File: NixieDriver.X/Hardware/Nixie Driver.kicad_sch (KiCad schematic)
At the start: 5 parts, among them J1 Conn_02x03_Odd_Even, J2 Conn_02x03_Odd_Even, J3 Conn_01x03, U1 PIC16F15243

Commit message: STM32L011F4U MCU
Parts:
- removed J1: Conn_02x03_Odd_Even, Connector_PinHeader_2.54mm:PinHeader_1x03_P2.54mm_Vertical, symbol Connector_Generic:Conn_01x03
- removed J2: Conn_02x03_Odd_Even, Connector_PinHeader_2.54mm:PinHeader_1x04_P2.54mm_Vertical, symbol Connector_Generic:Conn_01x04
- removed U1: PIC16F15243, Package_DFN_QFN:VQFN-20-1EP_3x3mm_P0.4mm_EP1.7x1.7mm, symbol MCU_Microchip_PIC16_:PIC16F15243-E/REB
- added J1: SWD, Connectory_PCB_Edge_:Tag-Connect EVC3-06, symbol Connector_Generic:Conn_01x06
- added J4, J5: Conn_01x03, Connector_PinHeader_2.54mm:PinHeader_1x02_P2.54mm_Vertical, symbol Connector_Generic:Conn_01x02
- added R13: 2.2k, Resistor_SMD:R_0603_1608Metric, symbol Device:R_US
- added U2: STM32L011F4Ux, Package_DFN_QFN:ST_UFQFPN-20_3x3mm_P0.5mm, symbol MCU_ST_STM32L0:STM32L011F4Ux
- J3: footprint Connector_PinHeader_2.54mm:PinHeader_1x03_P2.54mm_Vertical -> Connector_PinHeader_2.54mm:PinHeader_1x02_P2.54mm_Vertical; symbol Connector_Generic:Conn_01x03 -> Connector_Generic:Conn_01x02
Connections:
- net Driver_0: now also U2.9 (PA6)
- net Driver_1: now also U2.7 (PA4)
- net Driver_2: now also U2.6 (PA1)
- net Driver_3: now also U2.5 (PA0)
- net Driver_4: now also U2.1 (PC14)
- net Driver_5: now also U2.20 (PB9)
- net Driver_6: now also U2.15 (PA10)
- net Driver_7: now also U2.14 (PA9)
- net Driver_8: now also U2.11 (PB1)
- net Driver_9: now also U2.10 (PA7)
- net Driver_Dot: now also U2.8 (PA5)
- net GND: now also J1.5 (Pin_5), U2.12 (VSS)
- net SCL: now also J4.2 (Pin_2), U2.18 (PB6)
- net SDA: now also J4.1 (Pin_1), U2.19 (PB7)
- net Vdd: now also J1.1 (Pin_1), J5.1 (Pin_1), R13.2, U2.13 (VDD), U2.4 (VDDA); no longer J3.2 (Pin_2)
- net Vnn: now also J3.2 (Pin_2); no longer J3.3 (Pin_3)
- new net ADDR: J5.2 (Pin_2), R13.1, U2.2 (PC15)
- new net NRST: J1.3 (Pin_3), U2.3 (NRST)
- new net SWCLK: J1.4 (Pin_4), U2.17 (PA14)
- new net SWDIO: J1.2 (Pin_2), U2.16 (PA13)
- new net SWO: J1.6 (Pin_6)

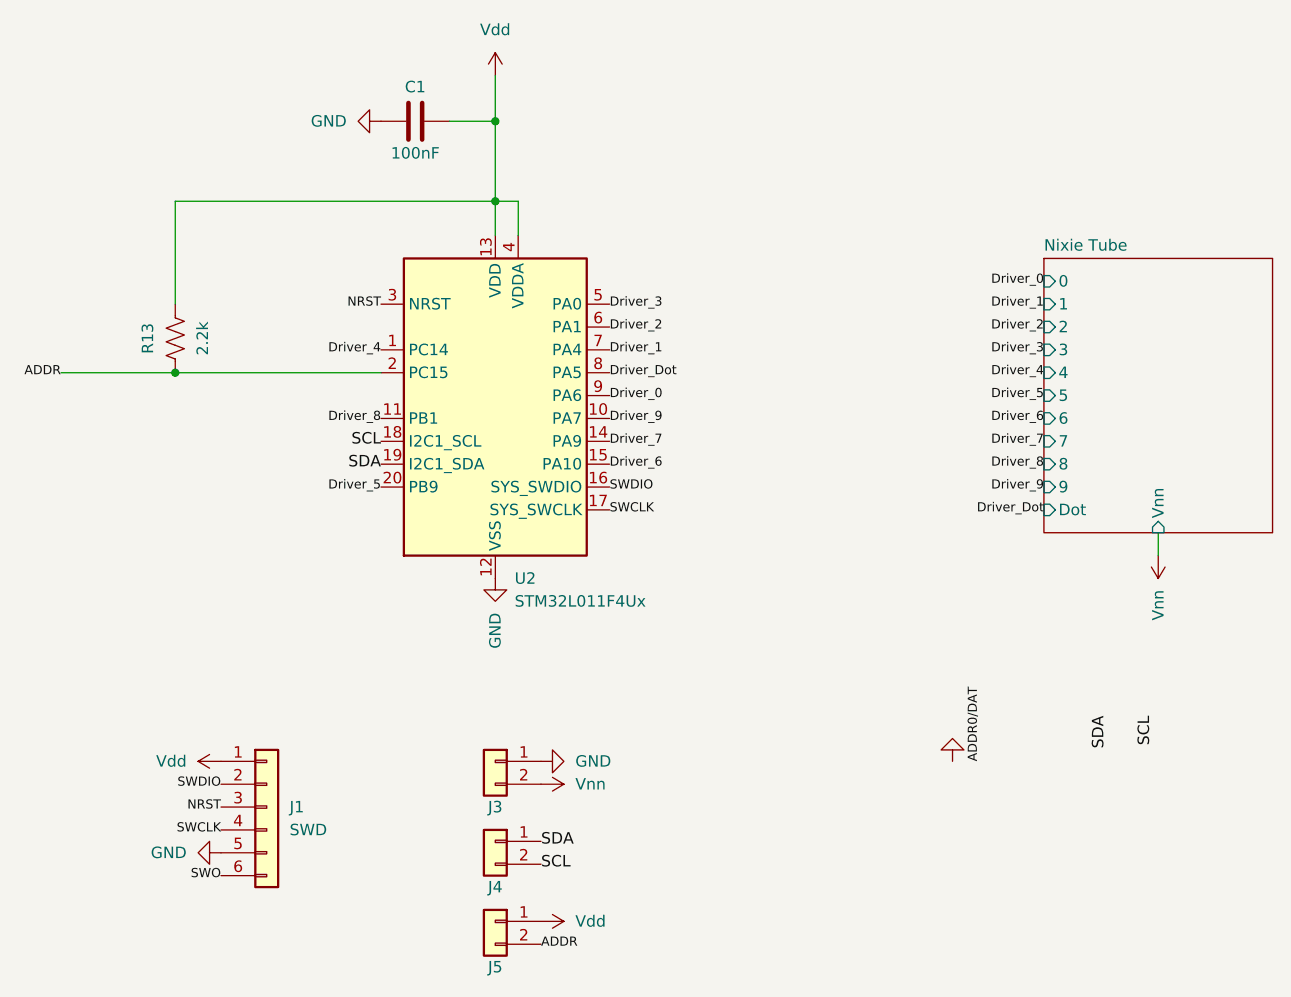
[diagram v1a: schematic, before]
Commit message: Switched to pin assignments that will actually work.
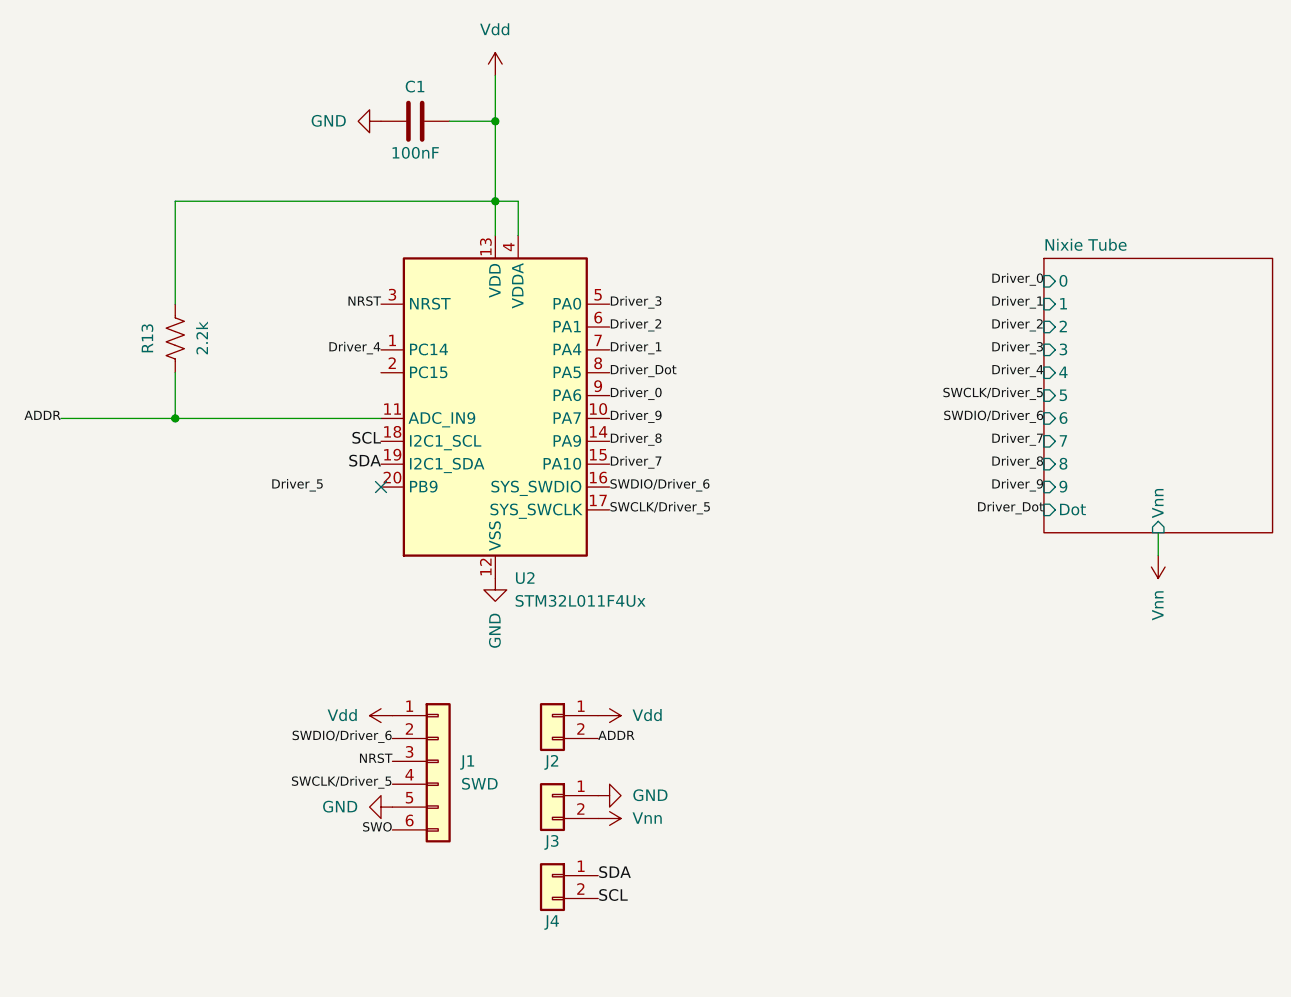
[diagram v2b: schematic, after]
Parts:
- renumbered J5 to J2
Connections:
- net Driver_6 is gone; now on net Driver_7: U2.15 (PA10)
- net ADDR: now also U2.11 (PB1); no longer U2.2 (PC15)
- net Driver_5: no longer U2.20 (PB9)
- net Driver_7: no longer U2.14 (PA9)
- net Driver_8: now also U2.14 (PA9); no longer U2.11 (PB1)
- net SWCLK renamed SWCLK/Driver_5
- net SWDIO renamed SWDIO/Driver_6
- no-connect marks 0 -> 1
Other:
- moved on the sheet: J1, J2, J3, J4

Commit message: Switched to 2mm pitch header
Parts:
- J2, J3, J4: footprint Connector_PinHeader_2.54mm:PinHeader_1x02_P2.54mm_Vertical -> Connector_PinHeader_2.00mm:PinHeader_1x02_P2.00mm_Vertical
- renumbered U2 to U1
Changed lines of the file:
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@@
 			)
 		)
-		(property "Footprint" "Connector_PinHeader_2.54mm:PinHeader_1x02_P2.54mm_Vertical"
+		(property "Footprint" "Connector_PinHeader_2.00mm:PinHeader_1x02_P2.00mm_Vertical"
 			(at 118.11 144.78 0)
 			(hide yes)
@@
 		(dnp no)
 		(fields_autoplaced yes)
-		(property "Reference" "U2"
+		(property "Reference" "U1"
 			(at 113.9033 111.76 0)
 			(show_name no)
@@
 			(project "Nixie Driver"
 				(path "/a603c7dd-0964-4ab1-bdb5-8ff7833b36d7"
-					(reference "U2")
+					(reference "U1")
 					(unit 1)
 				)
@@
 			)
 		)
-		(property "Footprint" "Connector_PinHeader_2.54mm:PinHeader_1x02_P2.54mm_Vertical"
+		(property "Footprint" "Connector_PinHeader_2.00mm:PinHeader_1x02_P2.00mm_Vertical"
 			(at 118.11 135.89 0)
 			(hide yes)
@@
 			)
 		)
-		(property "Footprint" "Connector_PinHeader_2.54mm:PinHeader_1x02_P2.54mm_Vertical"
+		(property "Footprint" "Connector_PinHeader_2.00mm:PinHeader_1x02_P2.00mm_Vertical"
 			(at 118.11 127 0)
 			(hide yes)

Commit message: switch MCU to SMT32C5
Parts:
- J1: now left out of the parts list
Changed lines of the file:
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@@
 		(body_style 1)
 		(exclude_from_sim no)
-		(in_bom yes)
+		(in_bom no)
 		(on_board yes)
 		(in_pos_files yes)
@@
 		(size 25.4 30.48)
 		(exclude_from_sim no)
-		(in_bom yes)
-		(on_board yes)
-		(dnp no)
+		(in_bom no)
+		(on_board yes)
+		(dnp no)
